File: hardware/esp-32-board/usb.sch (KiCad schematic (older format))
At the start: 11 parts, among them J5 USB_B_Micro, Q1 BCR129S, U2 USBLC6-2SC6, U3 CP2102N-A01-GQFN28

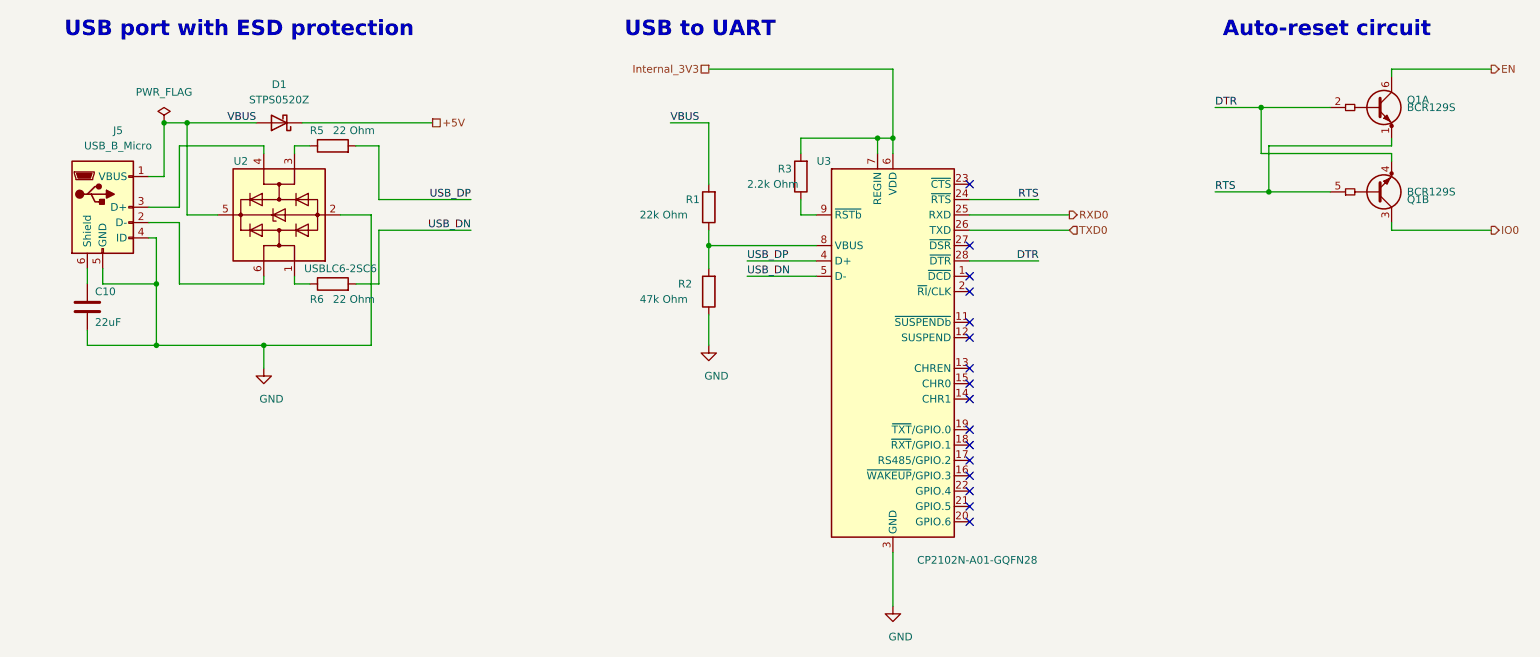
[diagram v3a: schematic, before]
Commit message: Use FT232RL instead of CP2102N
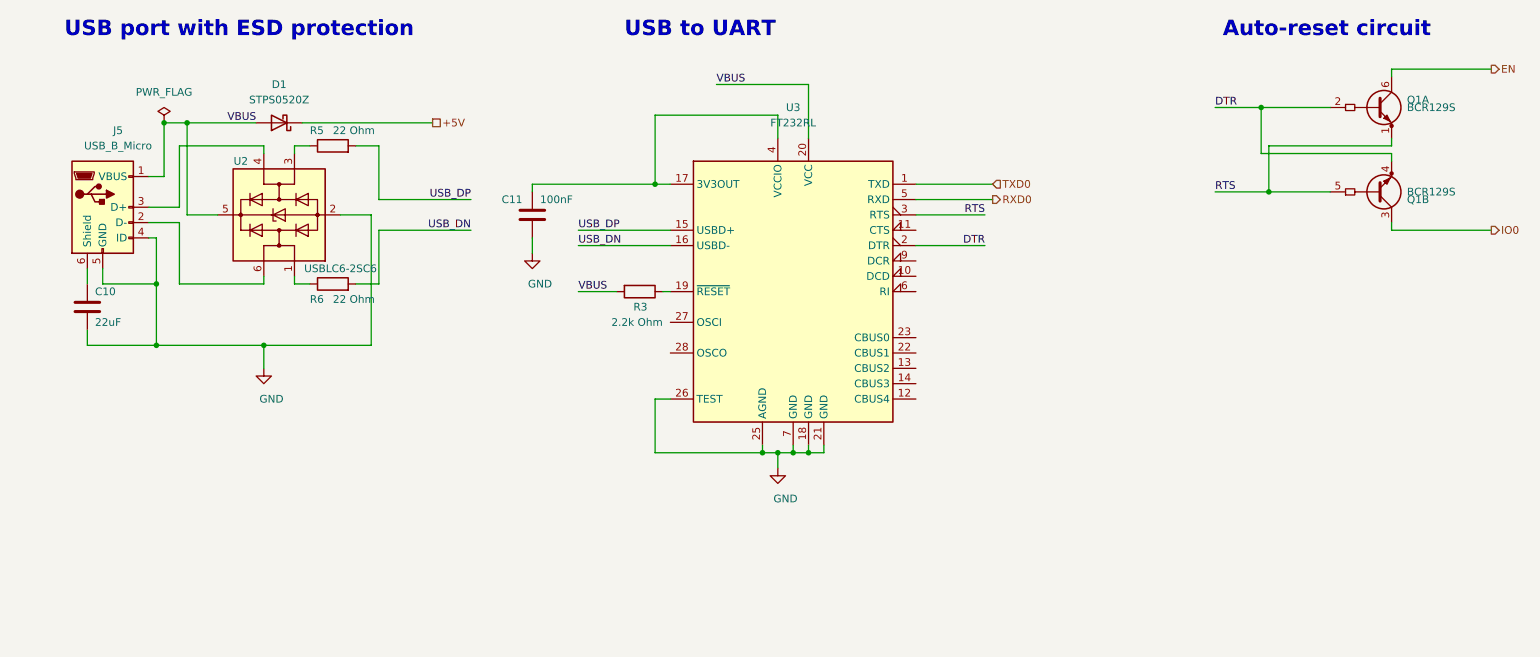
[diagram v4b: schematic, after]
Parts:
- removed R1: 22k Ohm, Resistor_SMD:R_0805_2012Metric_Pad1.20x1.40mm_HandSolder, symbol Device:R
- removed R2: 47k Ohm, Resistor_SMD:R_0805_2012Metric_Pad1.20x1.40mm_HandSolder, symbol Device:R
- removed U3: CP2102N-A01-GQFN28, Package_DFN_QFN:QFN-28-1EP_5x5mm_P0.5mm_EP3.35x3.35mm, symbol Interface_USB:CP2102N-A01-GQFN28
- added C11: 100nF, Capacitor_SMD:C_0805_2012Metric_Pad1.18x1.45mm_HandSolder, symbol Device:C
- added U3: FT232RL, Package_SO:SSOP-28_5.3x10.2mm_P0.65mm, symbol Interface_USB:FT232RL
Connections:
- net Internal_3V3 is gone; now on net VBUS: R3.2
- net DTR: now also U3.2 (DTR)
- net GND: now also C11.2, U3.18 (GND), U3.21 (GND), U3.25 (AGND), U3.26 (TEST), U3.7 (GND)
- net RTS: now also U3.3 (RTS)
- net RXD0: now also U3.5 (RXD)
- net TXD0: now also U3.1 (TXD)
- net USB_DN: now also U3.16 (USBD-)
- net USB_DP: now also U3.15 (USBD+)
- net VBUS: now also U3.20 (VCC)
- net at R3.1: now also U3.19 (~RESET~)
- new net: C11.1, U3.17 (3V3OUT), U3.4 (VCCIO)
- no-connect marks 16 -> 0
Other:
- moved on the sheet: R3
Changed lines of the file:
@@
 $EndDescr
-$Comp
-L Interface_USB:CP2102N-A01-GQFN28 U?
-U 1 1 5FFBA0ED
-P 6700 3700
-AR Path="/5FFBA0ED" Ref="U?"  Part="1"
-AR Path="/5FF73D59/5FFBA0ED" Ref="U3"  Part="1"
-F 0 "U3" H 6250 4950 50  0000 C CNN
-F 1 "CP2102N-A01-GQFN28" H 7250 2350 50  0000 C CNN
-F 2 "Package_DFN_QFN:QFN-28-1EP_5x5mm_P0.5mm_EP3.35x3.35mm" H 7150 2500 50  0001 L CNN
-F 3 "https://www.silabs.com/documents/public/data-sheets/cp2102n-datasheet.pdf" H 6750 2950 50  0001 C CNN
-F 4 "tme.eu" H 6700 3700 50  0001 C CNN "Vendor"
-F 5 "https://www.tme.eu/pl/details/cp2102-gm/uklady-scalone-interfejs-usb/silicon-labs/cp2102-gmr/" H 6700 3700 50  0001 C CNN "VendorLink"
-	1    6700 3700
-	1    0    0    -1
-$EndComp
 $Comp
 L power:GND #PWR?
 U 1 1 5FFBA0F3
-P 6700 5350
+P 5950 4450
 AR Path="/5FFBA0F3" Ref="#PWR?"  Part="1"
 AR Path="/5FF73D59/5FFBA0F3" Ref="#PWR025"  Part="1"
-F 0 "#PWR025" H 6700 5100 50  0001 C CNN
-F 1 "GND" H 6750 5150 50  0000 C CNN
-F 2 "" H 6700 5350 50  0001 C CNN
-F 3 "" H 6700 5350 50  0001 C CNN
-	1    6700 5350
-	1    0    0    -1
-$EndComp
-Wire Wire Line
-	7200 3100 7650 3100
-Wire Wire Line
-	7200 2700 7650 2700
-Text Label 7650 2700 2    50   ~ 0
+F 0 "#PWR025" H 5950 4200 50  0001 C CNN
+F 1 "GND" H 6000 4250 50  0000 C CNN
+F 2 "" H 5950 4450 50  0001 C CNN
+F 3 "" H 5950 4450 50  0001 C CNN
+	1    5950 4450
+	1    0    0    -1
+$EndComp
+Wire Wire Line
+	6850 3000 7300 3000
+Text Label 7300 2800 2    50   ~ 0
 RTS
 $Comp
 L Device:R R?
 U 1 1 5FFBA107
-P 6100 2550
+P 5050 3300
 AR Path="/5FFBA107" Ref="R?"  Part="1"
 AR Path="/5FF73D59/5FFBA107" Ref="R3"  Part="1"
-F 0 "R3" H 6250 2500 50  0000 R CNN
-F 1 "2.2k Ohm" H 6450 2600 50  0000 R CNN
-F 2 "Resistor_SMD:R_0805_2012Metric_Pad1.20x1.40mm_HandSolder" V 6030 2550 50  0001 C CNN
-F 3 "~" H 6100 2550 50  0001 C CNN
-F 4 "avt.pl" H 6100 2550 50  0001 C CNN "Vendor"
-F 5 "https://sklep.avt.pl/avt701-805.html" H 6100 2550 50  0001 C CNN "VendorLink"
-	1    6100 2550
-	-1   0    0    1
-$EndComp
-Wire Wire Line
-	6700 2400 6700 2300
-Wire Wire Line
-	6700 2300 6600 2300
-Connection ~ 6600 2300
-Wire Wire Line
-	6600 2300 6100 2300
-Wire Wire Line
-	6600 2300 6600 2400
-Connection ~ 6700 2300
-Wire Wire Line
-	6100 2800 6200 2800
-$Comp
-L Device:R R?
-U 1 1 5FFBA115
-P 5500 3300
-AR Path="/5FFBA115" Ref="R?"  Part="1"
-AR Path="/5FF73D59/5FFBA115" Ref="R2"  Part="1"
-F 0 "R2" H 5700 3250 50  0000 R CNN
-F 1 "47k Ohm" H 5950 3350 50  0000 R CNN
-F 2 "Resistor_SMD:R_0805_2012Metric_Pad1.20x1.40mm_HandSolder" V 5430 3300 50  0001 C CNN
-F 3 "~" H 5500 3300 50  0001 C CNN
-F 4 "avt.pl" H 5500 3300 50  0001 C CNN "Vendor"
-F 5 "https://sklep.avt.pl/avt701-805.html" H 5500 3300 50  0001 C CNN "VendorLink"
-	1    5500 3300
-	-1   0    0    1
-$EndComp
-Wire Wire Line
-	6200 3000 5500 3000
-Wire Wire Line
-	5500 3000 5500 3150
-$Comp
-L Device:R R?
-U 1 1 5FFBA123
-P 5500 2750
-AR Path="/5FFBA123" Ref="R?"  Part="1"
-AR Path="/5FF73D59/5FFBA123" Ref="R1"  Part="1"
-F 0 "R1" H 5650 2700 50  0000 R CNN
-F 1 "22k Ohm" H 5950 2800 50  0000 R CNN
-F 2 "Resistor_SMD:R_0805_2012Metric_Pad1.20x1.40mm_HandSolder" V 5430 2750 50  0001 C CNN
-F 3 "~" H 5500 2750 50  0001 C CNN
-F 4 "avt.pl" H 5500 2750 50  0001 C CNN "Vendor"
-F 5 "https://sklep.avt.pl/avt701-805.html" H 5500 2750 50  0001 C CNN "VendorLink"
-	1    5500 2750
-	-1   0    0    1
-$EndComp
-Wire Wire Line
-	5500 3000 5500 2900
-Connection ~ 5500 3000
-Wire Wire Line
-	5500 2600 5500 2200
-Wire Wire Line
-	6100 2300 6100 2400
-Wire Wire Line
-	6100 2700 6100 2800
-Text Label 5750 3100 0    50   ~ 0
+F 0 "R3" V 5150 3350 50  0000 R CNN
+F 1 "2.2k Ohm" V 5250 3450 50  0000 R CNN
+F 2 "Resistor_SMD:R_0805_2012Metric_Pad1.20x1.40mm_HandSolder" V 4980 3300 50  0001 C CNN
+F 3 "~" H 5050 3300 50  0001 C CNN
+F 4 "avt.pl" H 5050 3300 50  0001 C CNN "Vendor"
+F 5 "https://sklep.avt.pl/avt701-805.html" H 5050 3300 50  0001 C CNN "VendorLink"
+	1    5050 3300
+	0    1    1    0
+$EndComp
+Text Label 4650 2900 0    50   ~ 0
 USB_DP
-Text Label 5750 3200 0    50   ~ 0
+Text Label 4650 3000 0    50   ~ 0
 USB_DN
-Wire Wire Line
-	5750 3100 6200 3100
-Wire Wire Line
-	6200 3200 5750 3200
-NoConn ~ 7200 3200
-NoConn ~ 7200 3300
-NoConn ~ 7200 3600
-NoConn ~ 7200 3800
-NoConn ~ 7200 3900
-NoConn ~ 7200 4000
-NoConn ~ 7200 4500
-NoConn ~ 7200 4400
-NoConn ~ 7200 4300
-NoConn ~ 7200 4200
-NoConn ~ 7200 4800
-NoConn ~ 7200 4700
-NoConn ~ 7200 4600
-NoConn ~ 7200 2600
-NoConn ~ 7200 3000
-$Comp
-L power:GND #PWR?
-U 1 1 5FFBA14D
-P 5500 3650
-AR Path="/5FFBA14D" Ref="#PWR?"  Part="1"
-AR Path="/5FF73D59/5FFBA14D" Ref="#PWR024"  Part="1"
-F 0 "#PWR024" H 5500 3400 50  0001 C CNN
-F 1 "GND" H 5550 3450 50  0000 C CNN
-F 2 "" H 5500 3650 50  0001 C CNN
-F 3 "" H 5500 3650 50  0001 C CNN
-	1    5500 3650
-	1    0    0    -1
-$EndComp
-Wire Wire Line
-	5500 3450 5500 3650
 $Comp
 L Connector:USB_B_Micro J?
@@
 Wire Wire Line
 	2600 3800 2600 3650
-Wire Wire Line
-	5500 2200 5250 2200
-Text Label 5250 2200 0    50   ~ 0
+Text Label 5550 1950 0    50   ~ 0
 VBUS
 Text HLabel 10600 1850 2    50   Output ~ 0
@@
 Text HLabel 10600 2900 2    50   Output ~ 0
 IO0
-Text HLabel 7850 2900 2    50   Input ~ 0
+Text HLabel 7350 2600 2    50   Input ~ 0
 TXD0
-Text HLabel 7850 2800 2    50   Output ~ 0
+Text HLabel 7350 2700 2    50   Output ~ 0
 RXD0
-Wire Wire Line
-	7200 2800 7850 2800
-Wire Wire Line
-	7850 2900 7200 2900
-Text Label 7650 3100 2    50   ~ 0
+Text Label 7300 3000 2    50   ~ 0
 DTR
-Wire Wire Line
-	6700 5000 6700 5350
 Text Label 3950 2700 2    50   ~ 0
 USB_DP
-Text HLabel 5500 1850 0    50   UnSpc ~ 0
-Internal_3V3
-Wire Wire Line
-	5500 1850 6700 1850
-Wire Wire Line
-	6700 1850 6700 2300
 $Comp
 L Device:D_Schottky D?
@@
 Text Notes 8850 1650 0    100  ~ 20
 Auto-reset circuit
-NoConn ~ 7200 3500
 Wire Wire Line
 	1850 2550 1950 2550
@@
 Wire Wire Line
 	2800 3250 2900 3250
+Wire Wire Line
+	5550 1950 6150 1950
+Text Label 4650 3300 0    50   ~ 0
+VBUS
+Wire Wire Line
+	4650 3300 4900 3300
+Wire Wire Line
+	5200 3300 5250 3300
+Wire Wire Line
+	4650 3000 5250 3000
+Wire Wire Line
+	5950 2150 5950 2300
+Wire Wire Line
+	6150 1950 6150 2300
+$Comp
+L Interface_USB:FT232RL U3
+U 1 1 5FE99968
+P 6050 3300
+F 0 "U3" H 6050 4500 50  0000 C CNN
+F 1 "FT232RL" H 6050 4400 50  0000 C CNN
+F 2 "Package_SO:SSOP-28_5.3x10.2mm_P0.65mm" H 7150 2400 50  0001 C CNN
+F 3 "https://www.ftdichip.com/Support/Documents/DataSheets/ICs/DS_FT232R.pdf" H 6050 3300 50  0001 C CNN
+	1    6050 3300
+	1    0    0    -1
+$EndComp
+Wire Wire Line
+	4650 2900 5250 2900
+Wire Wire Line
+	6850 2800 7300 2800
+Wire Wire Line
+	6850 2600 7350 2600
+Wire Wire Line
+	6850 2700 7350 2700
+Wire Wire Line
+	5850 4300 5850 4350
+Wire Wire Line
+	5850 4350 5950 4350
+Wire Wire Line
+	5950 4350 5950 4450
+Wire Wire Line
+	5950 4350 6050 4350
+Wire Wire Line
+	6050 4350 6050 4300
+Connection ~ 5950 4350
+Wire Wire Line
+	6050 4350 6150 4350
+Wire Wire Line
+	6150 4350 6150 4300
+Connection ~ 6050 4350
+Wire Wire Line
+	6150 4350 6250 4350
+Wire Wire Line
+	6250 4350 6250 4300
+Connection ~ 6150 4350
+Wire Wire Line
+	5250 4000 5150 4000
+Wire Wire Line
+	5150 4000 5150 4350
+Wire Wire Line
+	5150 4350 5850 4350
+Connection ~ 5850 4350
+$Comp
+L Device:C C11
+U 1 1 5FEE7EEB
+P 4350 2800
+F 0 "C11" H 4150 2900 50  0000 L CNN
+F 1 "100nF" H 4400 2900 50  0000 L CNN
+F 2 "Capacitor_SMD:C_0805_2012Metric_Pad1.18x1.45mm_HandSolder" H 4388 2650 50  0001 C CNN
+F 3 "~" H 4350 2800 50  0001 C CNN
+	1    4350 2800
+	1    0    0    -1
+$EndComp
+Wire Wire Line
+	5250 2600 5150 2600
+Wire Wire Line
+	4350 2600 4350 2650
+Wire Wire Line
+	4350 2950 4350 3050
+$Comp
+L power:GND #PWR?
+U 1 1 5FEFF60F
+P 4350 3050
+AR Path="/5FEFF60F" Ref="#PWR?"  Part="1"
+AR Path="/5FF73D59/5FEFF60F" Ref="#PWR024"  Part="1"
+F 0 "#PWR024" H 4350 2800 50  0001 C CNN
+F 1 "GND" H 4400 2850 50  0000 C CNN
+F 2 "" H 4350 3050 50  0001 C CNN
+F 3 "" H 4350 3050 50  0001 C CNN
+	1    4350 3050
+	1    0    0    -1
+$EndComp
+Wire Wire Line
+	5150 2600 5150 2150
+Wire Wire Line
+	5150 2150 5950 2150
+Connection ~ 5150 2600
+Wire Wire Line
+	5150 2600 4350 2600
 $EndSCHEMATC

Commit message: Use FT232RL instead of CP2102N
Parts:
- C11: Vendor (none) -> avt.pl; VendorLink (none) -> https://sklep.avt.pl/zestaw-kondensatorow-smd-0805-720-sztu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
- U3: Vendor (none) -> tme.eu; VendorLink (none) -> https://www.tme.eu/pl/details/ft232rl/uklady-scalone-interf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
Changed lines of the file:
@@
 F 2 "Package_SO:SSOP-28_5.3x10.2mm_P0.65mm" H 7150 2400 50  0001 C CNN
 F 3 "https://www.ftdichip.com/Support/Documents/DataSheets/ICs/DS_FT232R.pdf" H 6050 3300 50  0001 C CNN
+F 4 "tme.eu" H 6050 3300 50  0001 C CNN "Vendor"
+F 5 "https://www.tme.eu/pl/details/ft232rl/uklady-scalone-interfejs-usb/ftdi/ft232rl-reel/" H 6050 3300 50  0001 C CNN "VendorLink"
 	1    6050 3300
 	1    0    0    -1
@@
 F 2 "Capacitor_SMD:C_0805_2012Metric_Pad1.18x1.45mm_HandSolder" H 4388 2650 50  0001 C CNN
 F 3 "~" H 4350 2800 50  0001 C CNN
+F 4 "avt.pl" H 4350 2800 50  0001 C CNN "Vendor"
+F 5 "https://sklep.avt.pl/zestaw-kondensatorow-smd-0805-720-sztuk.html" H 4350 2800 50  0001 C CNN "VendorLink"
 	1    4350 2800
 	1    0    0    -1

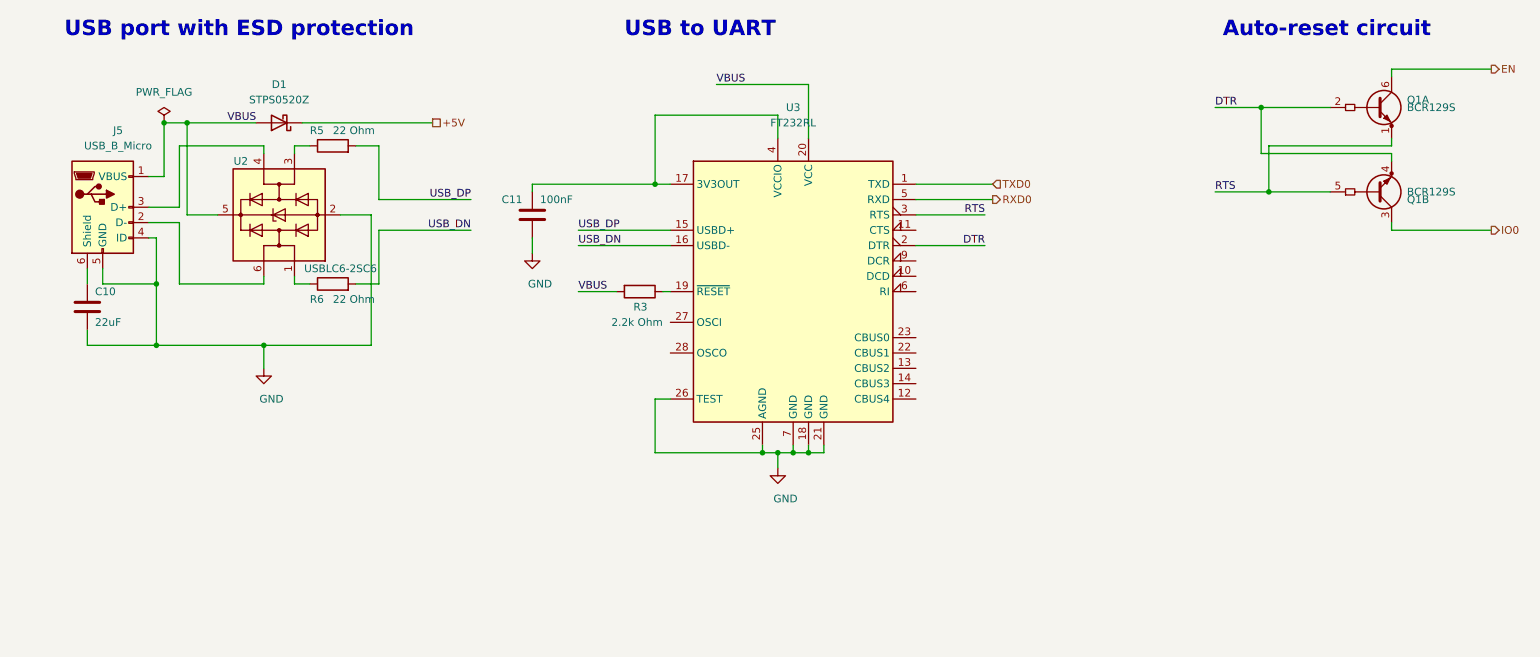
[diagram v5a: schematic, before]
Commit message: Fix ERC errors in schematic
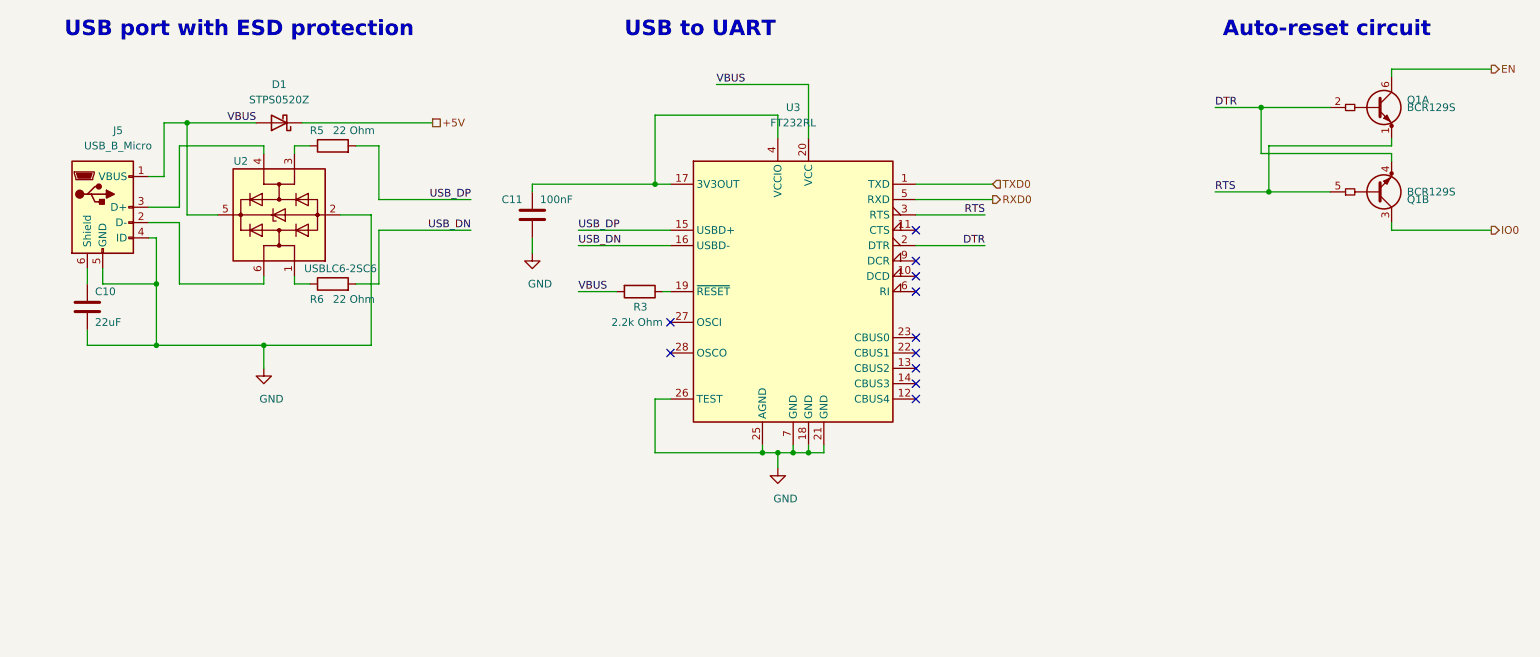
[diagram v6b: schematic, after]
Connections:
- no-connect marks 0 -> 11
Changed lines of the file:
@@
 Wire Wire Line
 	1850 2550 1950 2550
-$Comp
-L power:PWR_FLAG #FLG0104
-U 1 1 5FCE0047
-P 1950 2200
-F 0 "#FLG0104" H 1950 2275 50  0001 C CNN
-F 1 "PWR_FLAG" H 1950 2400 50  0000 C CNN
-F 2 "" H 1950 2200 50  0001 C CNN
-F 3 "~" H 1950 2200 50  0001 C CNN
-	1    1950 2200
-	1    0    0    -1
-$EndComp
 Wire Wire Line
 	1850 2950 1900 2950
@@
 Wire Wire Line
 	1950 2200 1950 2550
-Connection ~ 1950 2200
 Wire Wire Line
 	1850 2750 2050 2750
@@
 Wire Wire Line
 	5150 2600 4350 2600
+NoConn ~ 6850 2900
+NoConn ~ 6850 3100
+NoConn ~ 6850 3200
+NoConn ~ 6850 3300
+NoConn ~ 6850 3600
+NoConn ~ 6850 3700
+NoConn ~ 6850 3800
+NoConn ~ 6850 3900
+NoConn ~ 6850 4000
+NoConn ~ 5250 3500
+NoConn ~ 5250 3700
 $EndSCHEMATC
